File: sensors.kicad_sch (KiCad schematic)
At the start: 0 parts

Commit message: quick push, no major change
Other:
- note added: "ICM-42688-P"
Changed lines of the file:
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@@
 	(generator_version "9.0")
 	(paper "A4")
+	(text "ICM-42688-P\n"
+		(exclude_from_sim no)
+		(at 107.95 60.96 0)
+		(effects
+			(font
+				(size 1.27 1.27)
+			)
+		)
+	)
 )

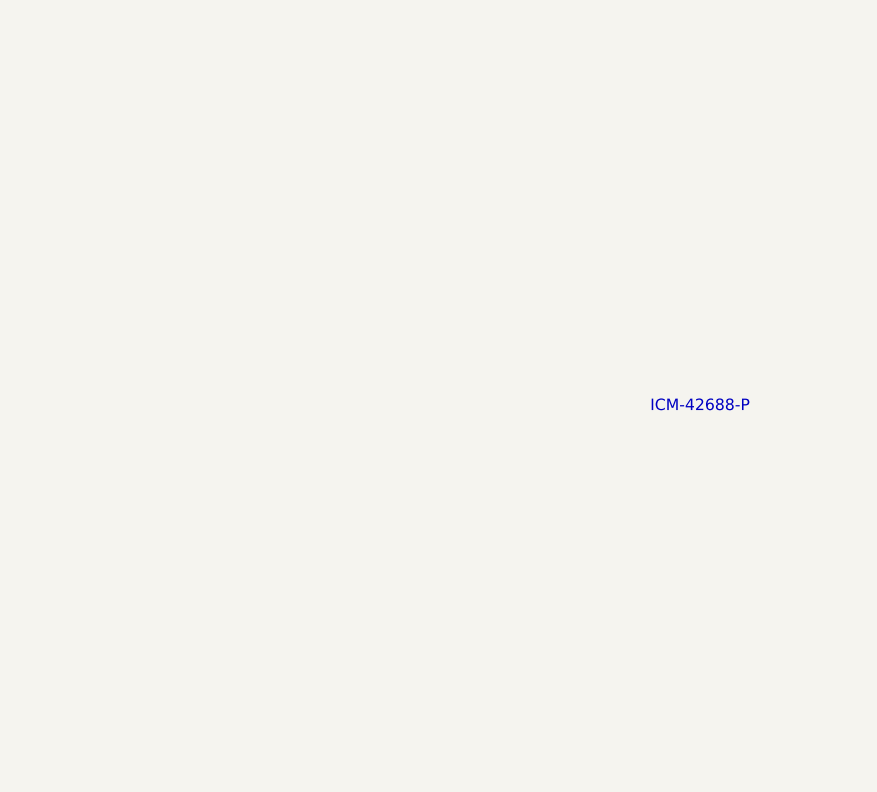
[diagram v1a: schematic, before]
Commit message: added second camera, 6-axis imu
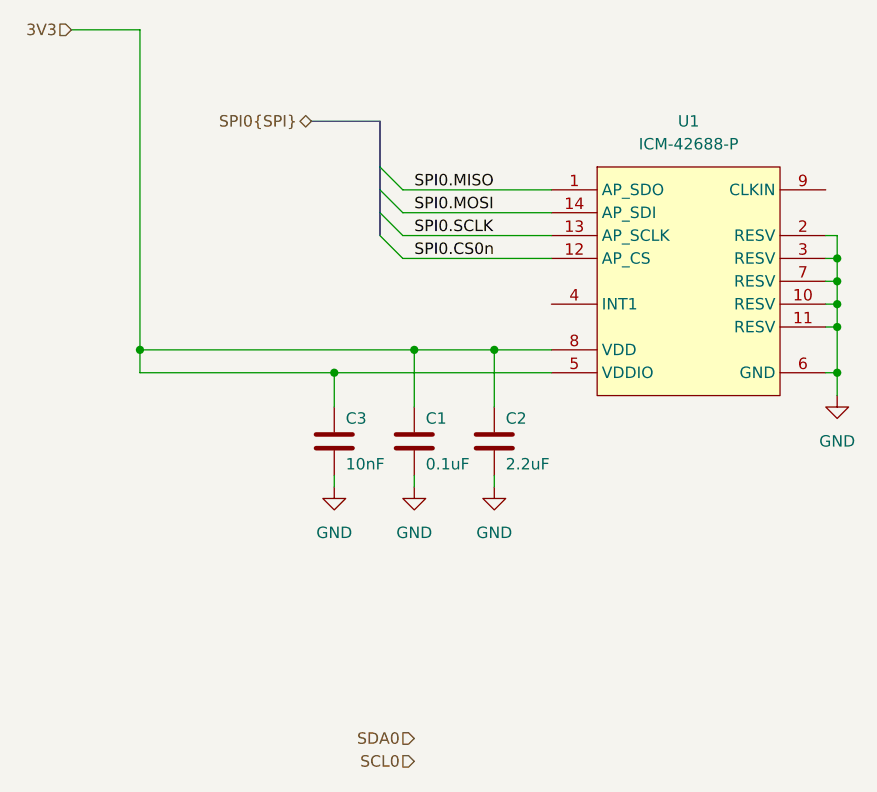
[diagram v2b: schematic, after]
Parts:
- added C1: 0.1uF, Capacitor_SMD:C_0402_1005Metric, symbol library:C
- added C2: 2.2uF, Capacitor_SMD:C_0402_1005Metric, symbol library:C
- added C3: 10nF, Capacitor_SMD:C_0402_1005Metric, symbol library:C
- added U1: ICM-42688-P, Package_LGA:LGA-14_3x2.5mm_P0.5mm_LayoutBorder3x4y, symbol library:ICM-42688-P
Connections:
- new net 3V3: C1.1, C2.1, C3.1, U1.5 (VDDIO), U1.8 (VDD)
- new net GND: C1.2, C2.2, C3.2, U1.10 (RESV), U1.11 (RESV), U1.2 (RESV), U1.3 (RESV), U1.6 (GND), U1.7 (RESV)
- new net SPI0.CS0n: U1.12 (AP_CS)
- new net SPI0.MISO: U1.1 (AP_SDO)
- new net SPI0.MOSI: U1.14 (AP_SDI)
- new net SPI0.SCLK: U1.13 (AP_SCLK)
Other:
- note removed: "ICM-42688-P"

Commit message: annotations, small fixes
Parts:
- renumbered C3 to C10, C1 to C11, C2 to C12, U1 to U3
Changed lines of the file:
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@@
 		(at 45.72 54.61)
 		(diameter 0)
-		(color 0 0 0 0)
+		(color 255 153 0 1)
 	)
 	(junction
 		(at 67.31 57.15)
 		(diameter 0)
-		(color 0 0 0 0)
+		(color 255 153 0 1)
 	)
 	(junction
@@
 		(at 76.2 54.61)
 		(diameter 0)
-		(color 0 0 0 0)
+		(color 255 153 0 1)
 	)
 	(junction
@@
 		(at 85.09 54.61)
 		(diameter 0)
-		(color 0 0 0 0)
+		(color 255 153 0 1)
 	)
 	(junction
@@
 		(dnp no)
 		(fields_autoplaced yes)
-		(property "Reference" "#PWR06"
+		(property "Reference" "#PWR023"
 			(at 85.09 76.2 0)
 			(effects
@@
 			(project "CUTIE-CITRUS"
 				(path "/40af415e-5e3a-41a5-ab07-08c2181863e4/66b6385f-f0c0-4feb-8706-85a19fc48611"
-					(reference "#PWR06")
+					(reference "#PWR023")
 					(unit 1)
 				)
@@
 		(on_board yes)
 		(dnp no)
-		(property "Reference" "C2"
+		(property "Reference" "C12"
 			(at 86.36 62.23 0)
 			(effects
@@
 			(project "CUTIE-CITRUS"
 				(path "/40af415e-5e3a-41a5-ab07-08c2181863e4/66b6385f-f0c0-4feb-8706-85a19fc48611"
-					(reference "C2")
+					(reference "C12")
 					(unit 1)
 				)
@@
 		(on_board yes)
 		(dnp no)
-		(property "Reference" "C3"
+		(property "Reference" "C10"
 			(at 68.58 62.23 0)
 			(effects
@@
 			(project "CUTIE-CITRUS"
 				(path "/40af415e-5e3a-41a5-ab07-08c2181863e4/66b6385f-f0c0-4feb-8706-85a19fc48611"
-					(reference "C3")
+					(reference "C10")
 					(unit 1)
 				)
@@
 		(on_board yes)
 		(dnp no)
-		(property "Reference" "C1"
+		(property "Reference" "C11"
 			(at 77.47 62.23 0)
 			(effects
@@
 			(project "CUTIE-CITRUS"
 				(path "/40af415e-5e3a-41a5-ab07-08c2181863e4/66b6385f-f0c0-4feb-8706-85a19fc48611"
-					(reference "C1")
+					(reference "C11")
 					(unit 1)
 				)
@@
 		(dnp no)
 		(fields_autoplaced yes)
-		(property "Reference" "#PWR09"
+		(property "Reference" "#PWR022"
 			(at 76.2 76.2 0)
 			(effects
@@
 			(project "CUTIE-CITRUS"
 				(path "/40af415e-5e3a-41a5-ab07-08c2181863e4/66b6385f-f0c0-4feb-8706-85a19fc48611"
-					(reference "#PWR09")
+					(reference "#PWR022")
 					(unit 1)
 				)
@@
 		(dnp no)
 		(fields_autoplaced yes)
-		(property "Reference" "U1"
+		(property "Reference" "U3"
 			(at 106.68 29.21 0)
 			(effects
@@
 			(project ""
 				(path "/40af415e-5e3a-41a5-ab07-08c2181863e4/66b6385f-f0c0-4feb-8706-85a19fc48611"
-					(reference "U1")
+					(reference "U3")
 					(unit 1)
 				)
@@
 		(dnp no)
 		(fields_autoplaced yes)
-		(property "Reference" "#PWR05"
+		(property "Reference" "#PWR020"
 			(at 123.19 66.04 0)
 			(effects
@@
 			(project ""
 				(path "/40af415e-5e3a-41a5-ab07-08c2181863e4/66b6385f-f0c0-4feb-8706-85a19fc48611"
-					(reference "#PWR05")
+					(reference "#PWR020")
 					(unit 1)
 				)
@@
 		(dnp no)
 		(fields_autoplaced yes)
-		(property "Reference" "#PWR07"
+		(property "Reference" "#PWR021"
 			(at 67.31 76.2 0)
 			(effects
@@
 			(project "CUTIE-CITRUS"
 				(path "/40af415e-5e3a-41a5-ab07-08c2181863e4/66b6385f-f0c0-4feb-8706-85a19fc48611"
-					(reference "#PWR07")
+					(reference "#PWR021")
 					(unit 1)
 				)

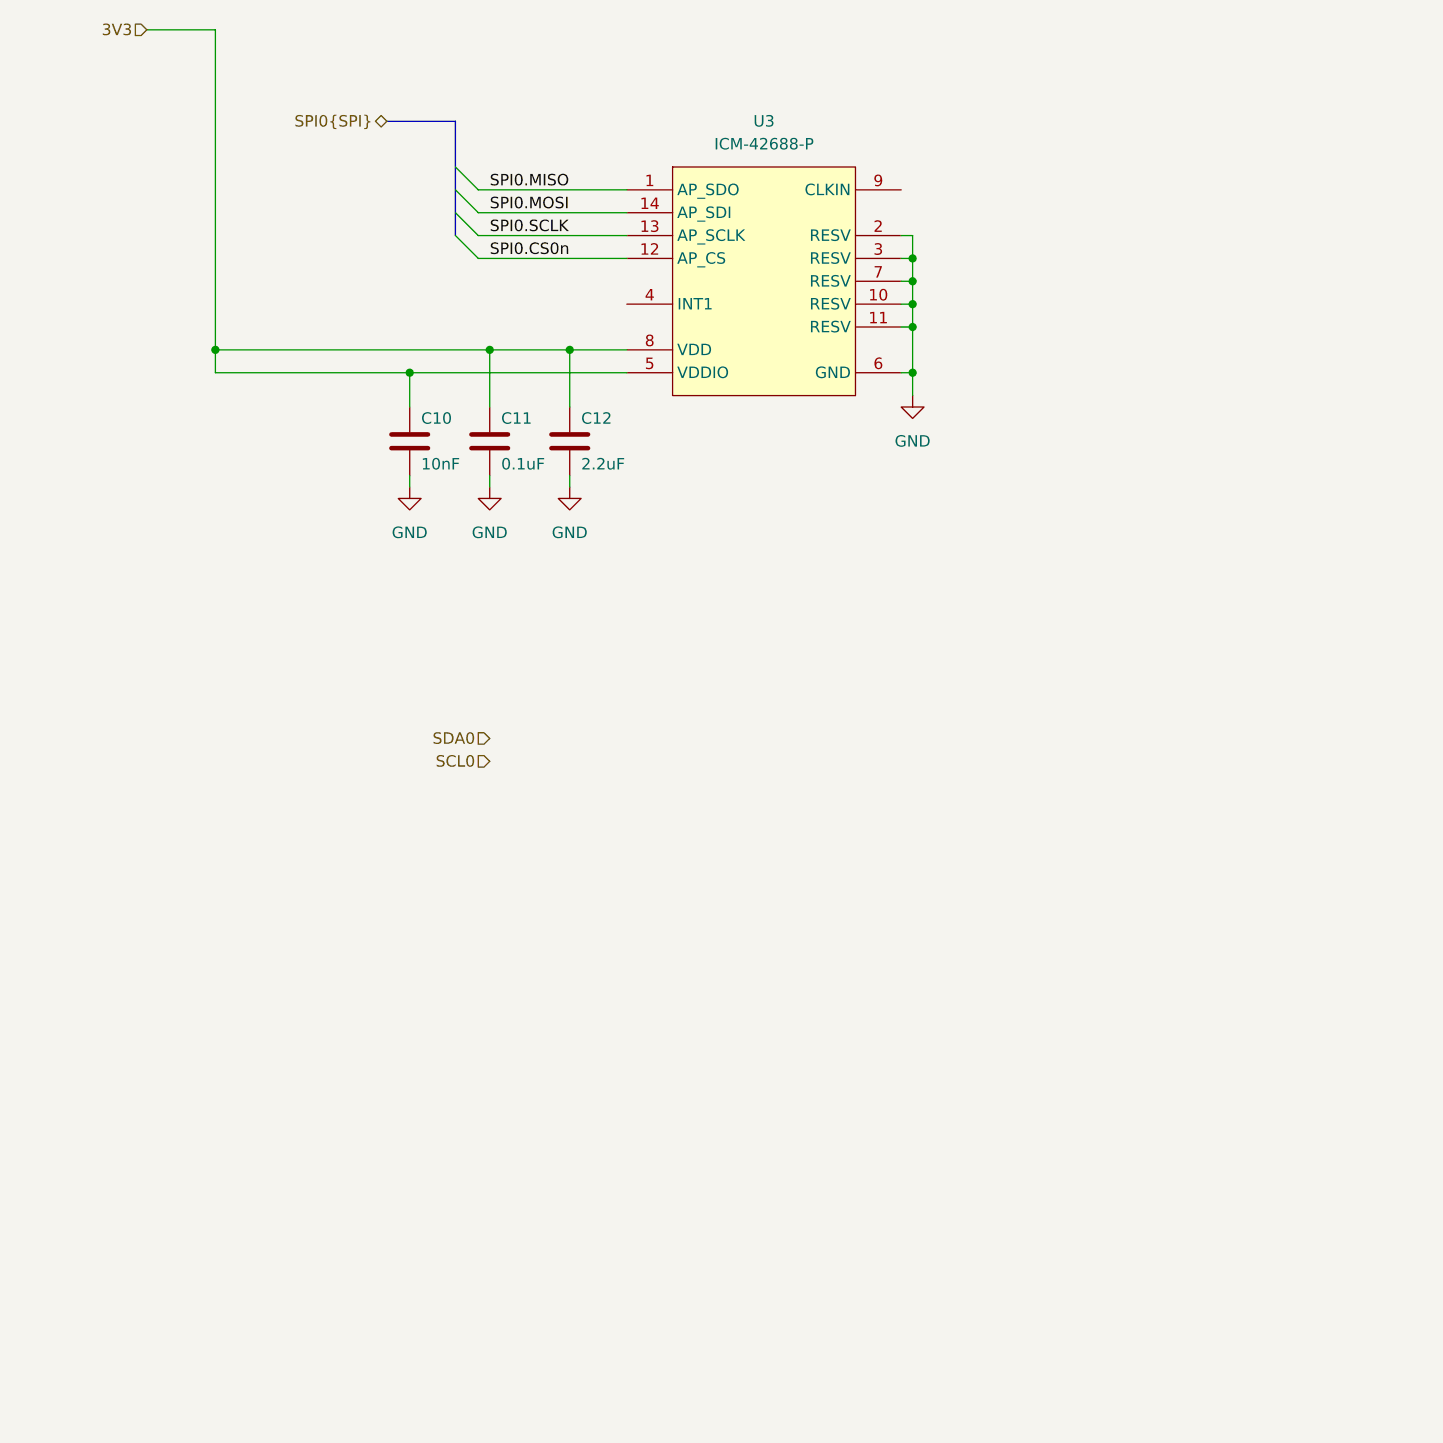
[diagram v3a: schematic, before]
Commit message: extra abstraction layer for cm5 conns.
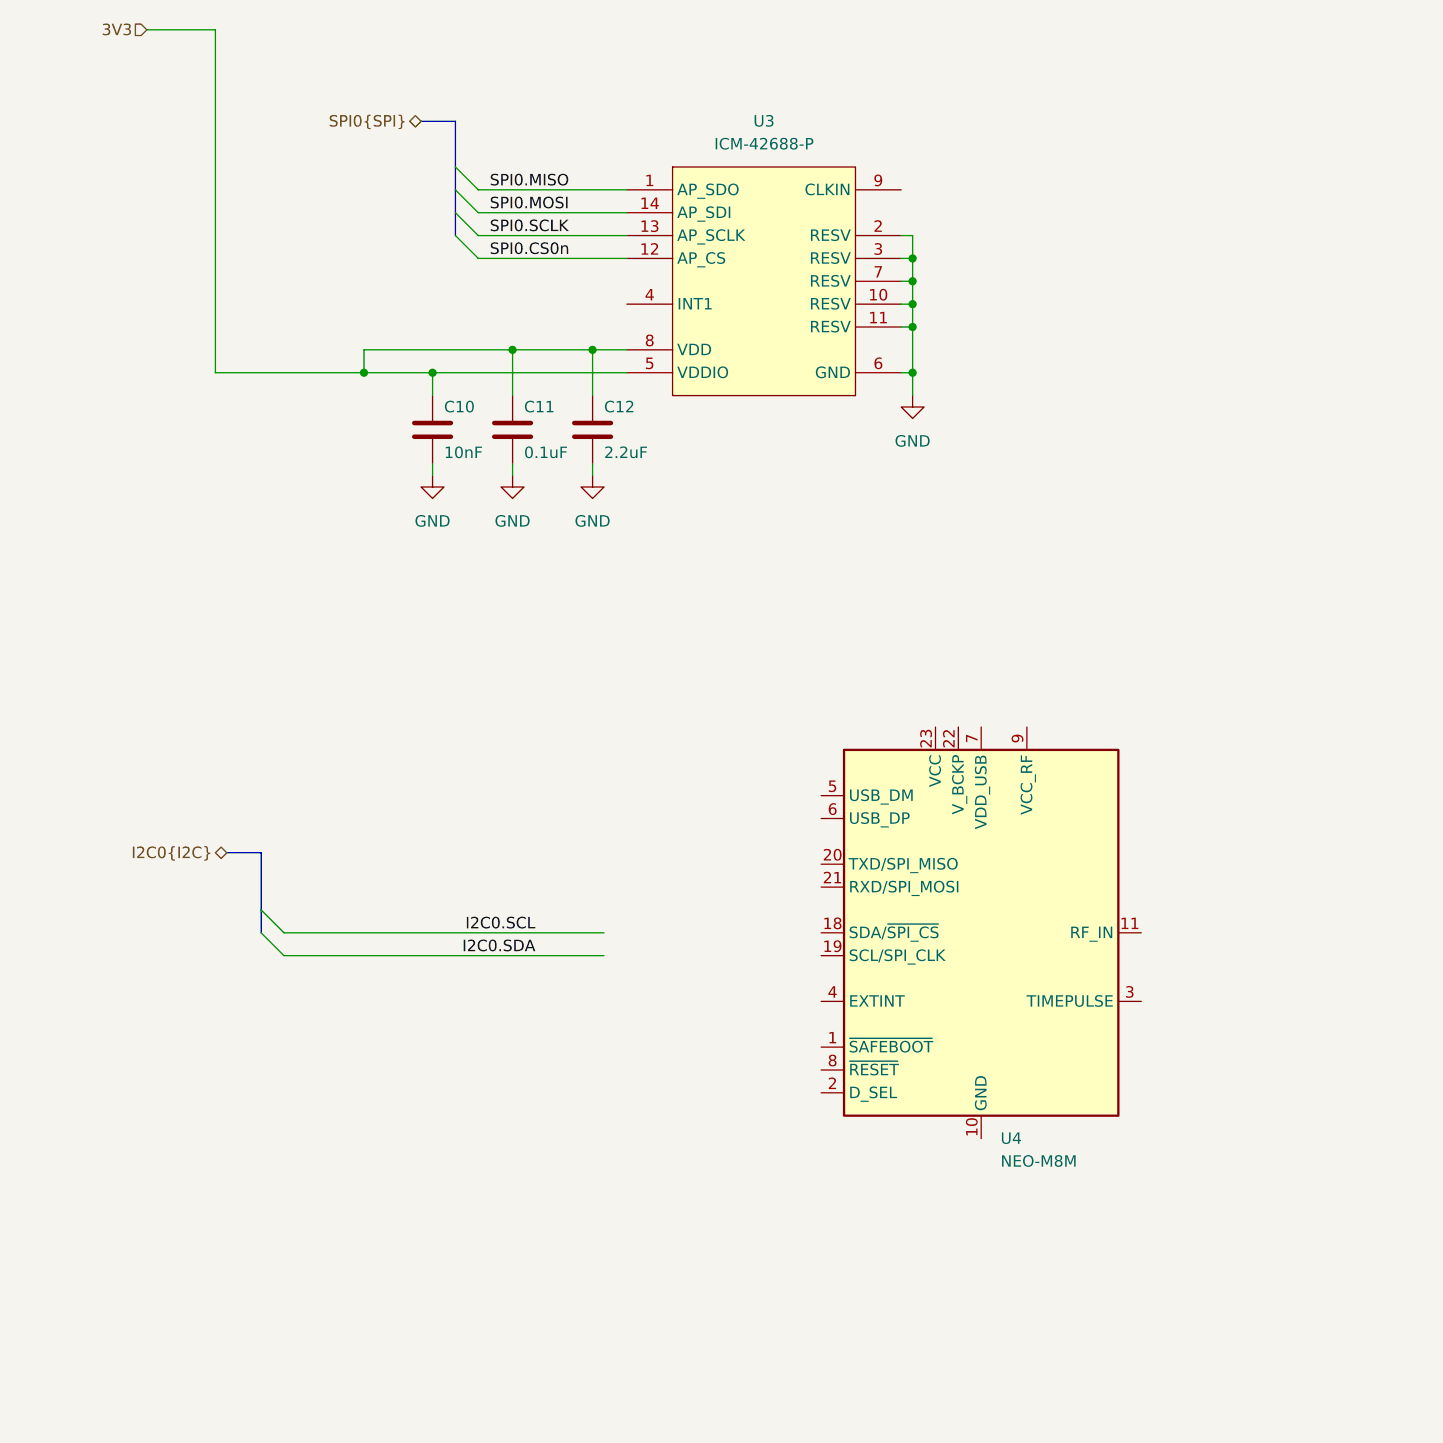
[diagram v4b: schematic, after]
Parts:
- added U4: NEO-M8M, RF_GPS:ublox_NEO, symbol RF_GPS:NEO-M8M
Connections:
- new net: U4.10 (GND), U4.12 (GND), U4.13 (GND), U4.24 (GND)
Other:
- company: (none) -> Andre S Winkel | Highlander Space Program | University of California, Riverside
- title: (none) -> CUTIE-CITRUS PCB
- moved on the sheet: C10, C11, C12

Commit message: neo m8m impl.
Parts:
- added C13: 47pF, symbol Device:C
- added C14: 0.1uF, Capacitor_SMD:C_0402_1005Metric, symbol library:C
- added C15: 2.2uF, Capacitor_SMD:C_0402_1005Metric, symbol library:C
- added C16: 1uF, Capacitor_SMD:C_0402_1005Metric, symbol library:C
- added D4: TPD1E05U06DPY, Package_SON:Texas_DPY0002A_0.6x1mm_P0.65mm, symbol Power_Protection:TPD1E05U06DPY
- added J4: Hirose U.FL, Connector_Coaxial:U.FL_Hirose_U.FL-R-SMT-1_Vertical, symbol Connector:Conn_Coaxial
- added TP18, TP19, TP20: TestPoint, TestPoint:TestPoint_Pad_D1.0mm, symbol Connector:TestPoint
- renumbered C11 to C10, C12 to C11, C10 to C12
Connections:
- net 3V3: now also U4.22 (V_BCKP), U4.23 (VCC), C14.1, C15.1, C16.1
- net GND: now also U3.9 (CLKIN), U4.10 (GND), U4.14 (RESERVED), U4.2 (D_SEL), U4.7 (VDD_USB), C14.2, C15.2, C16.2, D4.2 (GND), J4.2 (Ext)
- net SPI0.MISO: now also U4.20 (TXD/SPI_MISO)
- net SPI0.MOSI: now also U4.21 (RXD/SPI_MOSI)
- net SPI0.SCLK: now also U4.19 (SCL/SPI_CLK)
- net at U4.1 (~{SAFEBOOT}): now also TP19.1
- net at U4.12 (GND), U4.13 (GND), U4.24 (GND): no longer U4.10 (GND)
- net at U4.11 (RF_IN): now also C13.1
- net at U4.15 (RESERVED): now also U4.16 (RESERVED), U4.17 (RESERVED)
- net SPI0.CS1n: now reaches U4.18 (SDA/~{SPI_CS})
- net at U4.3 (TIMEPULSE): now also TP18.1
- net at U4.8 (~{RESET}): now also TP20.1
- new net: C13.2, D4.1 (I/O), J4.1 (In)
- no-connect marks 0 -> 5
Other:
- moved on the sheet: C10, C11, U4
